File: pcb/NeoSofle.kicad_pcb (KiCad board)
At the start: 2 copper layers, 141.3 x 117.6 mm, 71 parts, among them J1 JST_ACH_BM02B-ACHSS-GAN-ETF_S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, SW1 CPG135001S30, SW10 CPG135001S30, SW11 CPG135001S30, SW12 CPG135001S30, SW13 CPG135001S30, SW14 CPG135001S30, SW15 CPG135001S30, SW16 CPG135001S30, SW17 CPG135001S30, SW18 CPG135001S30, SW19 CPG135001S30, SW2 CPG135001S30, SW20 CPG135001S30, SW21 CPG135001S30, SW22 CPG135001S30, SW23 CPG135001S30, SW24 CPG135001S30, SW25 RotaryEncoder_Switch, SW26 CPG135001S30, SW27 CPG135001S30, SW28 CPG135001S30, SW29 CPG135001S30, SW3 CPG135001S30, SW30 CPG135001S30, SW4 CPG135001S30, SW5 CPG135001S30, SW6 CPG135001S30, SW7 CPG135001S30, SW8 CPG135001S30, SW9 CPG135001S30, U1 nice!nano v2

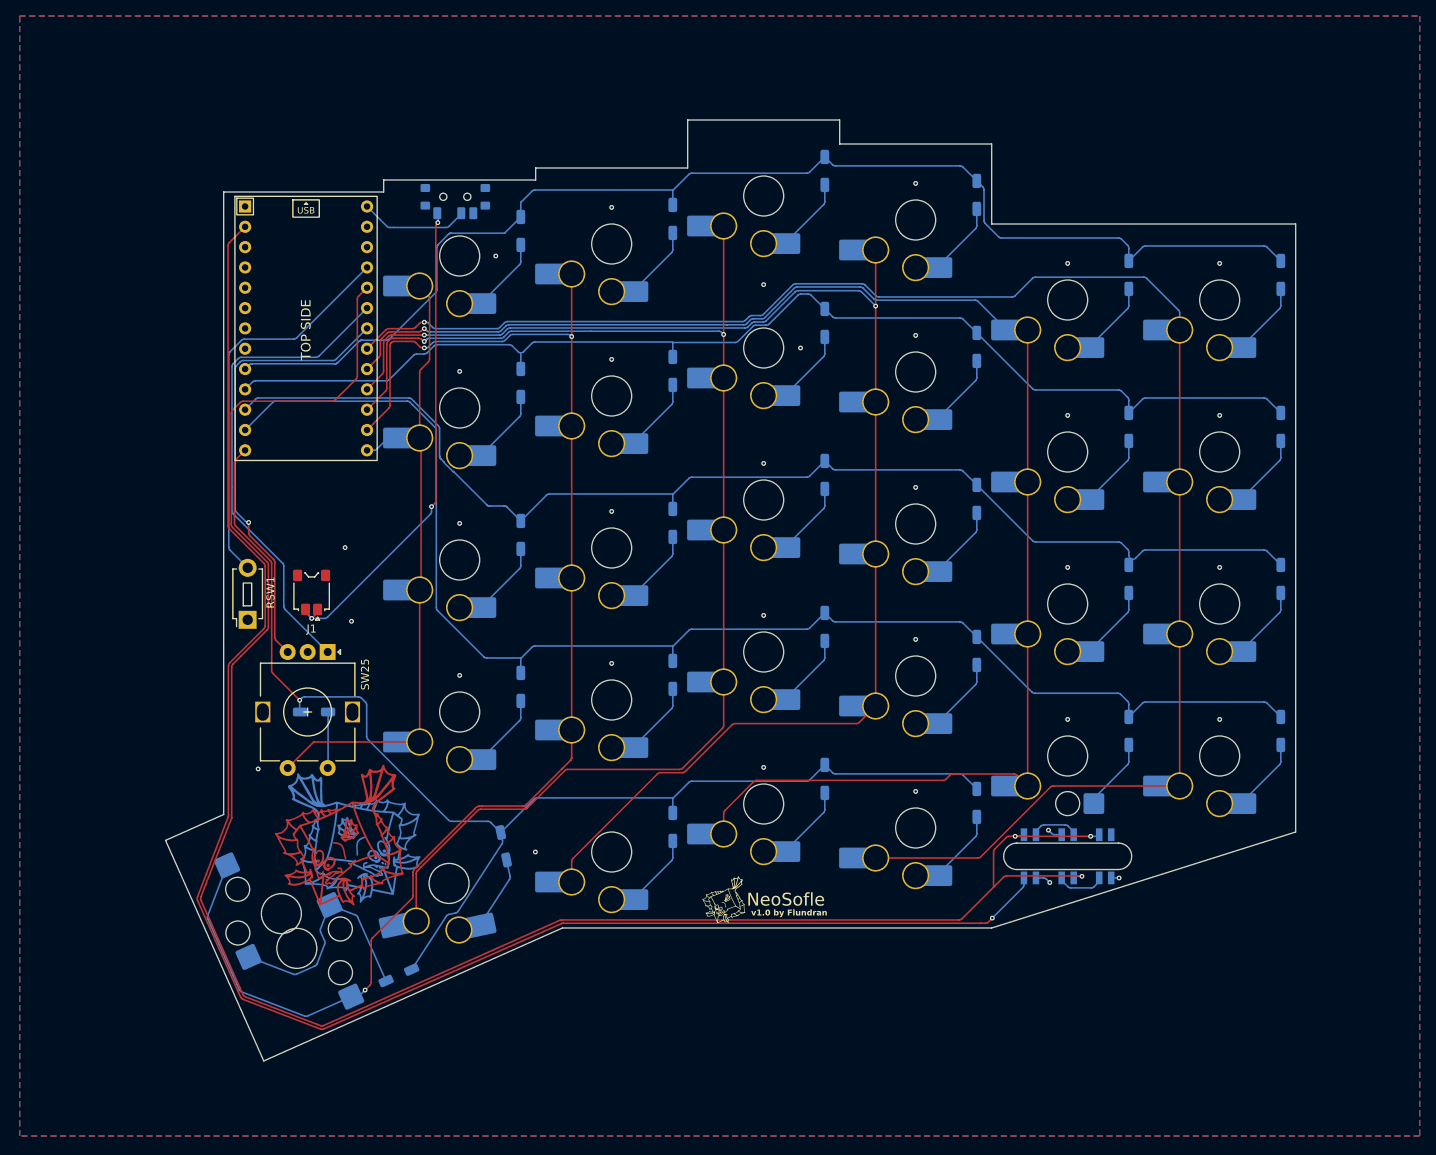
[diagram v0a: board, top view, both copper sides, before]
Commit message: Reposition JST battery connector to center and improve cord reachability.
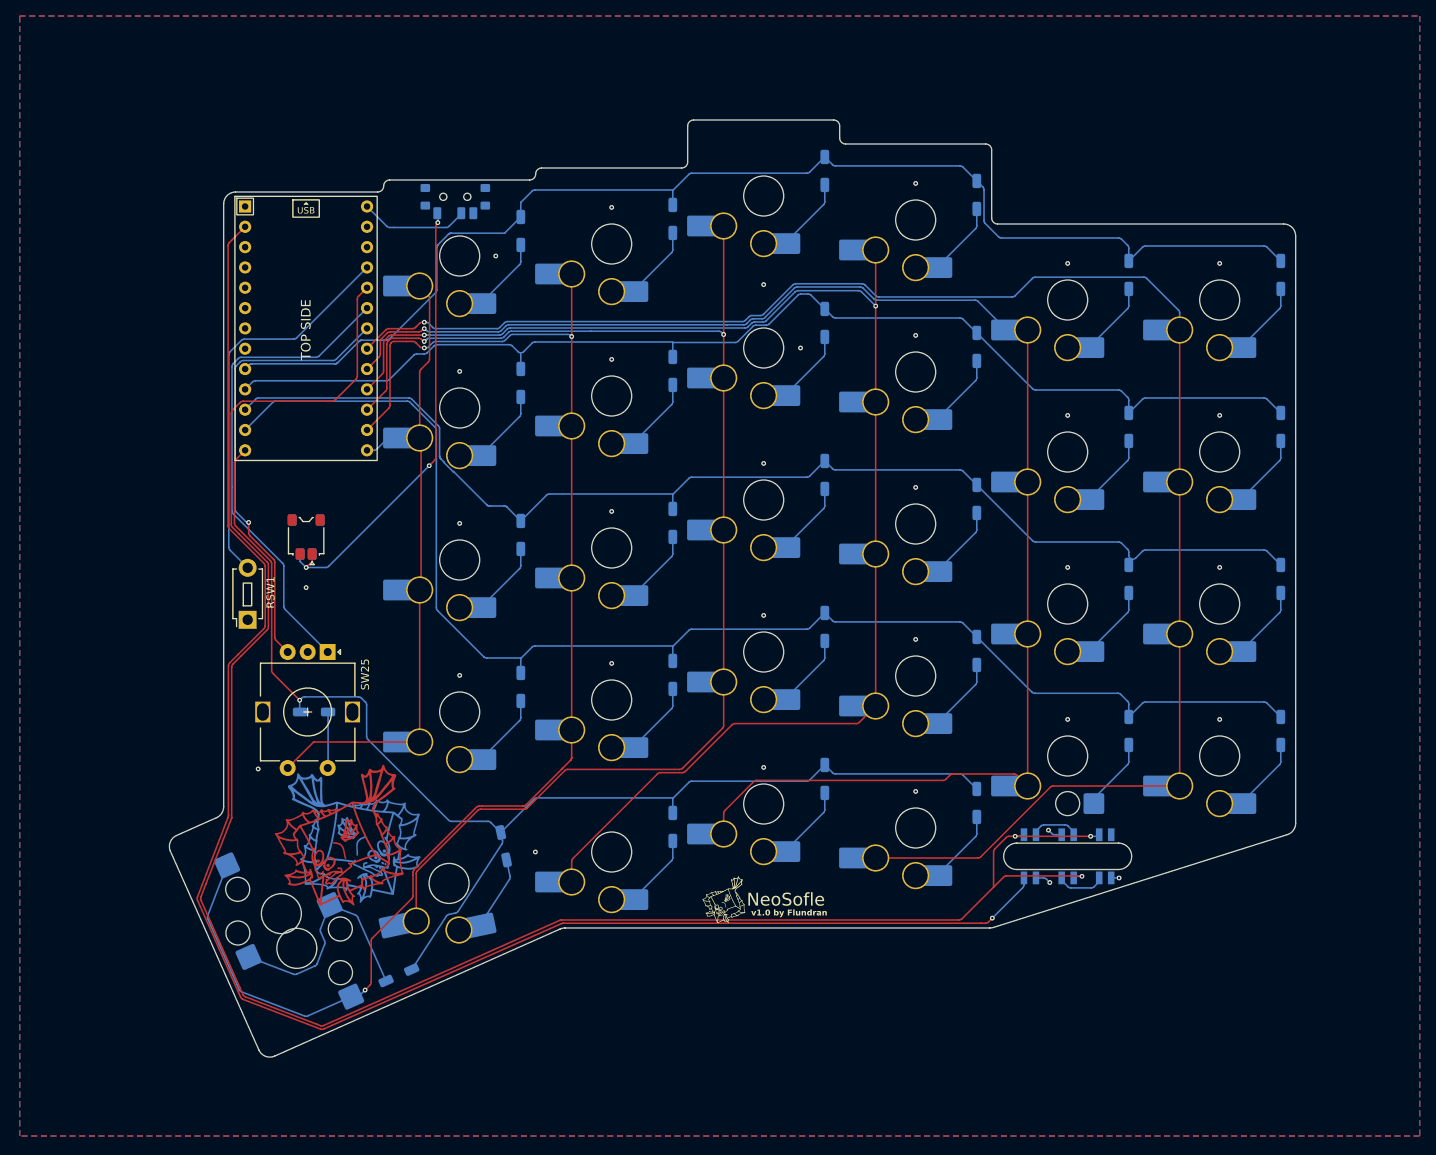
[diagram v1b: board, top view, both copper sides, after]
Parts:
- moved J1 6.96 mm to (141.6, 137.2)
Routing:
- net /BAT+: track 60.3 -> 56.6 mm
- net GND: vias 33 -> 32
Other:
- board size 141.3 x 117.6 mm -> 140.8 x 117.1 mm

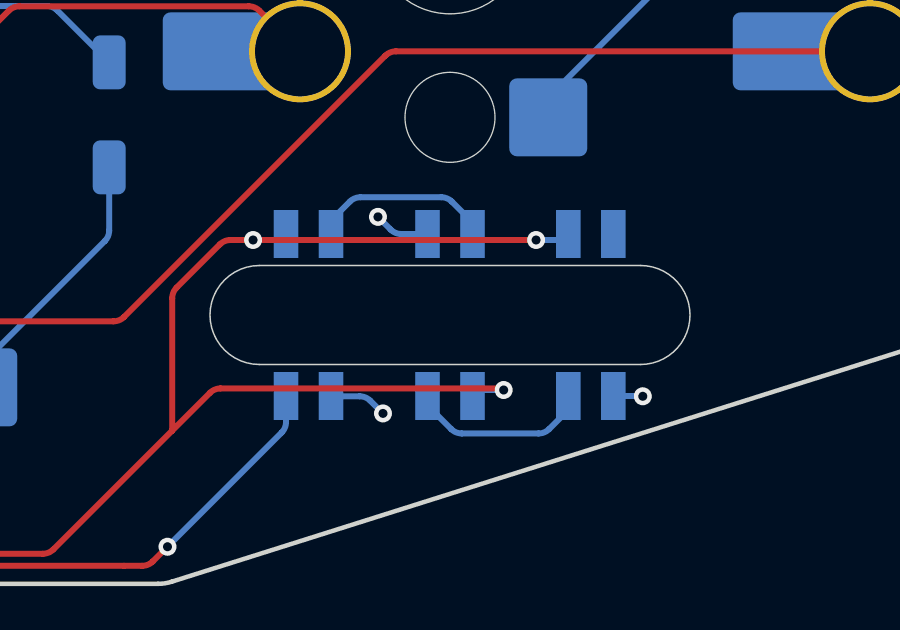
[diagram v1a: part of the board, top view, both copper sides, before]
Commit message: Correct LED cutout width to 3.4 mm.
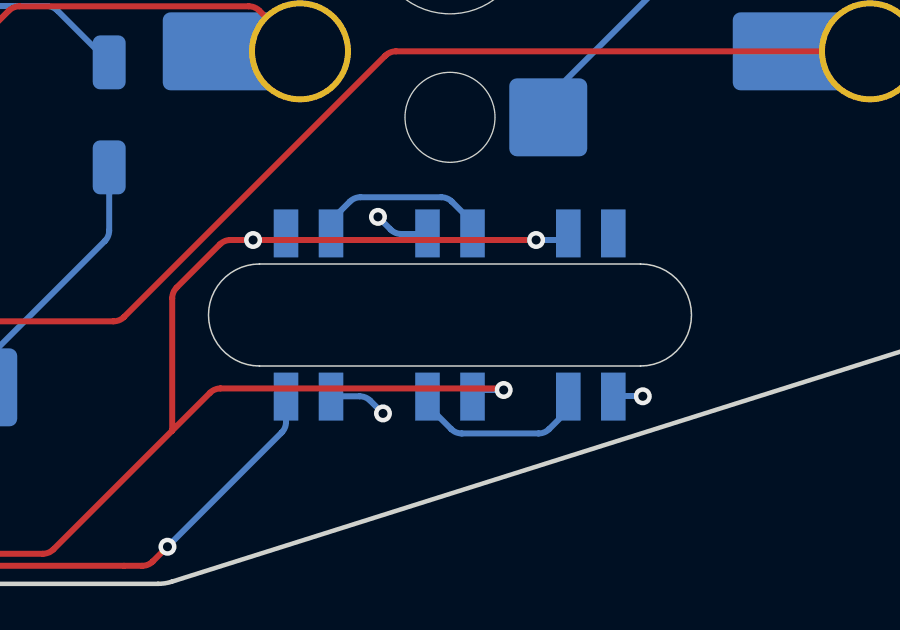
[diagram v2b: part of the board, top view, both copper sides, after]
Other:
- outline, holes or cut-outs redrawn

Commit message: Update RotaryEncoder footprint to alternatively support soldered choc v2 switch. Update pcb for new hybrid footprint. Remove NiceNano silk screen lines that were too close.
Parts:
- SW25: footprint NeoSofle:RotaryEncoder_Bourns_PEC11L-Switch_Vertical15mm -> NeoSofle:RotaryEncoder_Bourns_PEC11L_Vertical15mm_SW_ChocV2_Hybrid
- moved D25 7.14 mm to (147.4, 164.3), turned to -90 degrees
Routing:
- net Net-(LED1-DOUT): track 6.13 -> 4.92 mm
- net Net-(LED2-DOUT): track 6.09 -> 4.95 mm
- net Net-(D25-A): track 6.95 -> 6.00 mm
- net /ROW4: track 158.2 -> 157.5 mm, vias 1 -> 3
- net /COL5: track 77.7 -> 78.3 mm

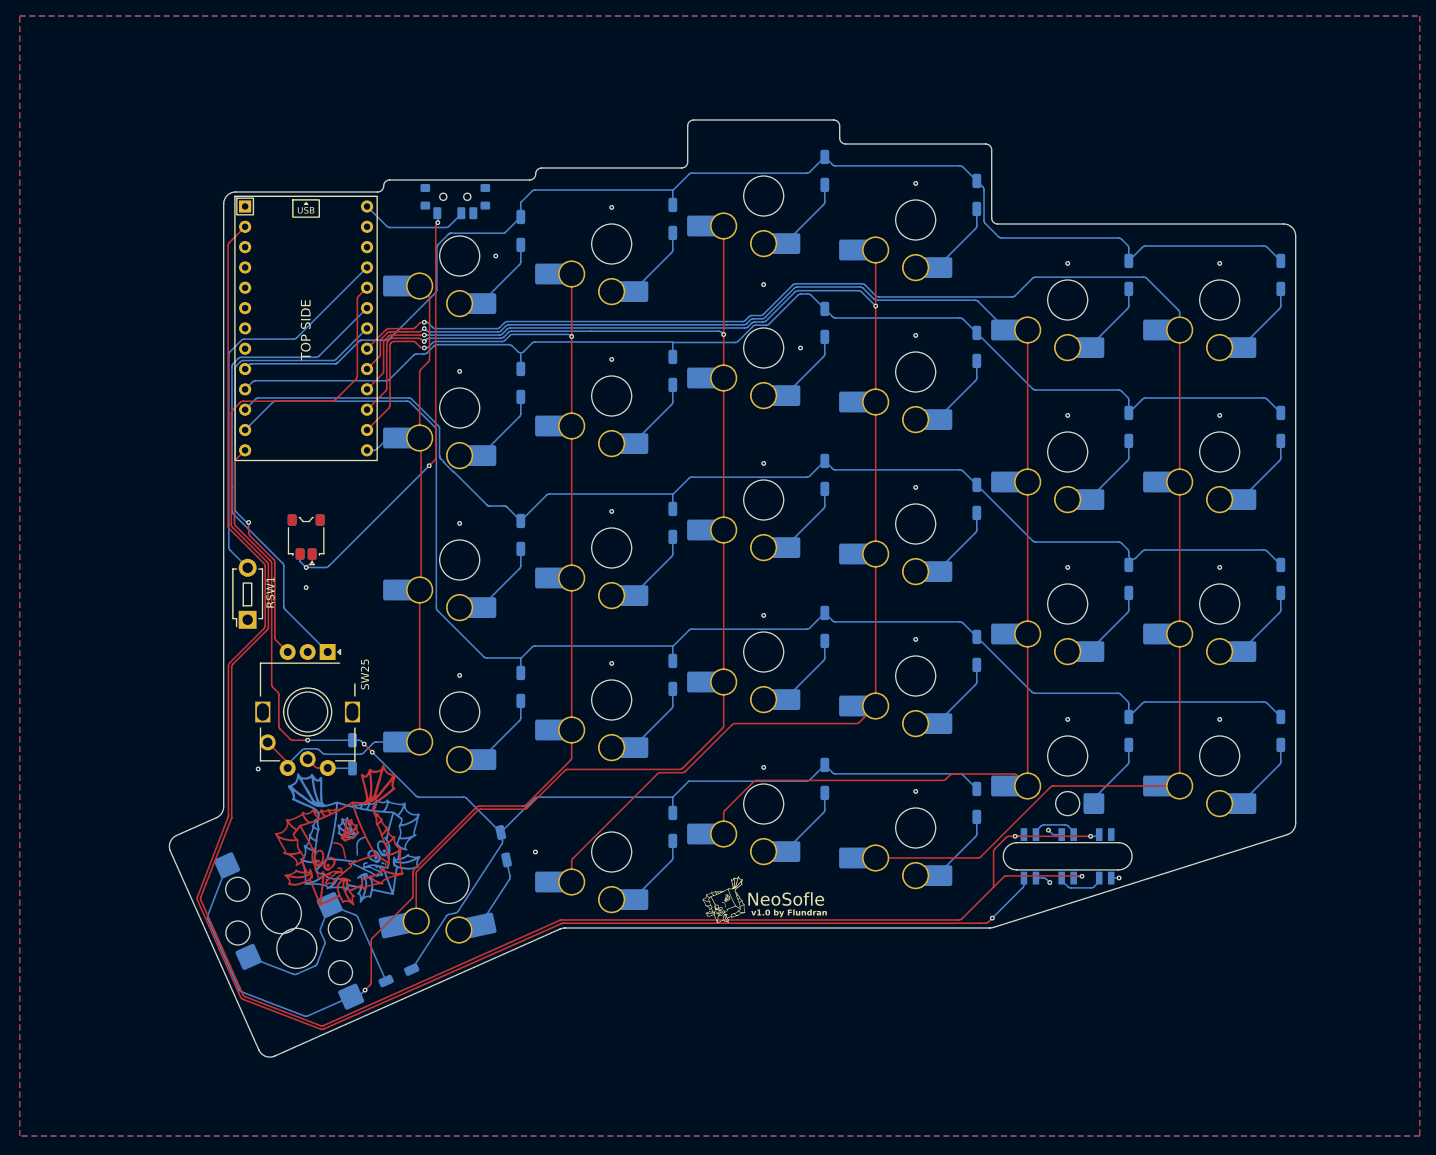
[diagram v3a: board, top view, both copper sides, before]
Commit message: Slightly increase margin of two outer thumbkeys. Remove todo-item about increasing top margin of mcu, won't do this since extruding USB contact should be fine or preferred when use with case.
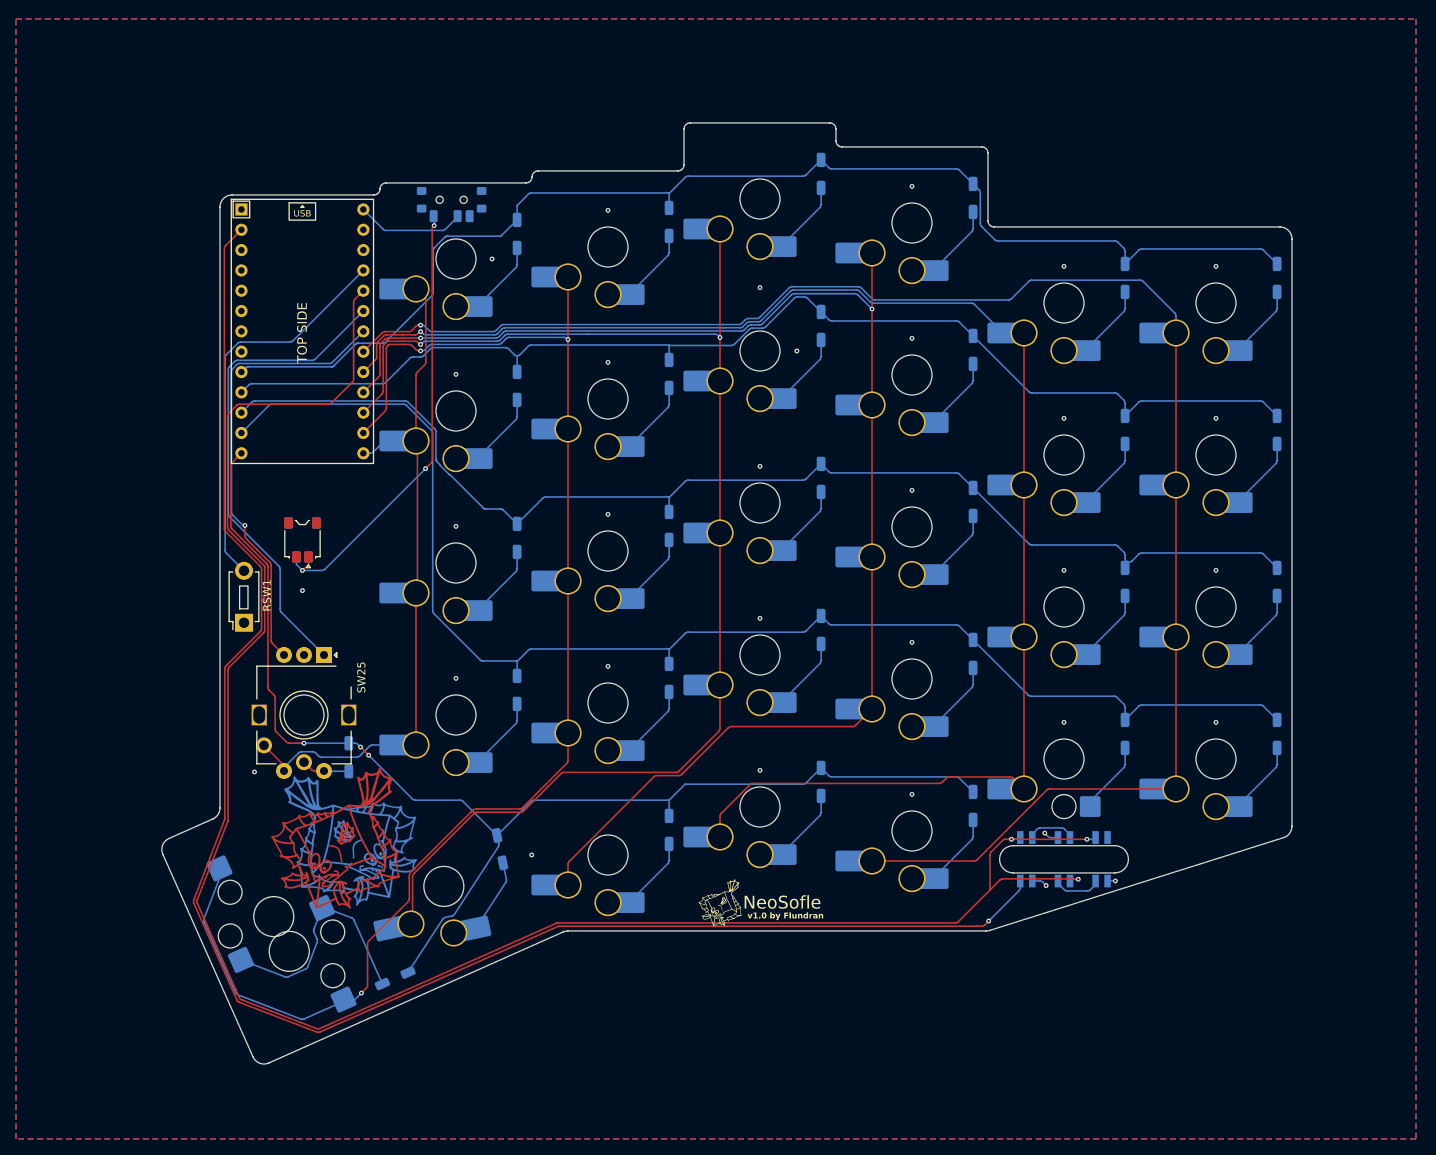
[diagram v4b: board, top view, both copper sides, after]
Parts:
- moved SW26 1.02 mm to (137.5, 184.6)
- moved SW27 0.75 mm to (158.8, 180.9)
- moved REF** 0.59 mm to (146.4, 175.8)
- moved D27 0.59 mm to (165.8, 176.2)
- moved LED1 0.59 mm to (231.6, 177.5)
- moved LED3 0.59 mm to (241.0, 177.5)
- moved D14 0.59 mm to (187.0, 135.8)
- moved D16 0.59 mm to (225.0, 132.8)
- moved D20 0.59 mm to (187.0, 154.8)
- moved D23 0.59 mm to (244.0, 161.8)
- moved D4 0.59 mm to (225.0, 94.8)
- moved SW18 0.59 mm to (255.3, 145.9)
- moved SW28 0.59 mm to (179.3, 176.9)
- moved SW29 0.59 mm to (198.3, 170.9)
- moved SW9 0.59 mm to (198.3, 113.9)
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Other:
- board size 140.8 x 117.1 mm -> 141.3 x 117.6 mm
